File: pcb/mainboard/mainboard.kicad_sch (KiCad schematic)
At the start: 0 parts

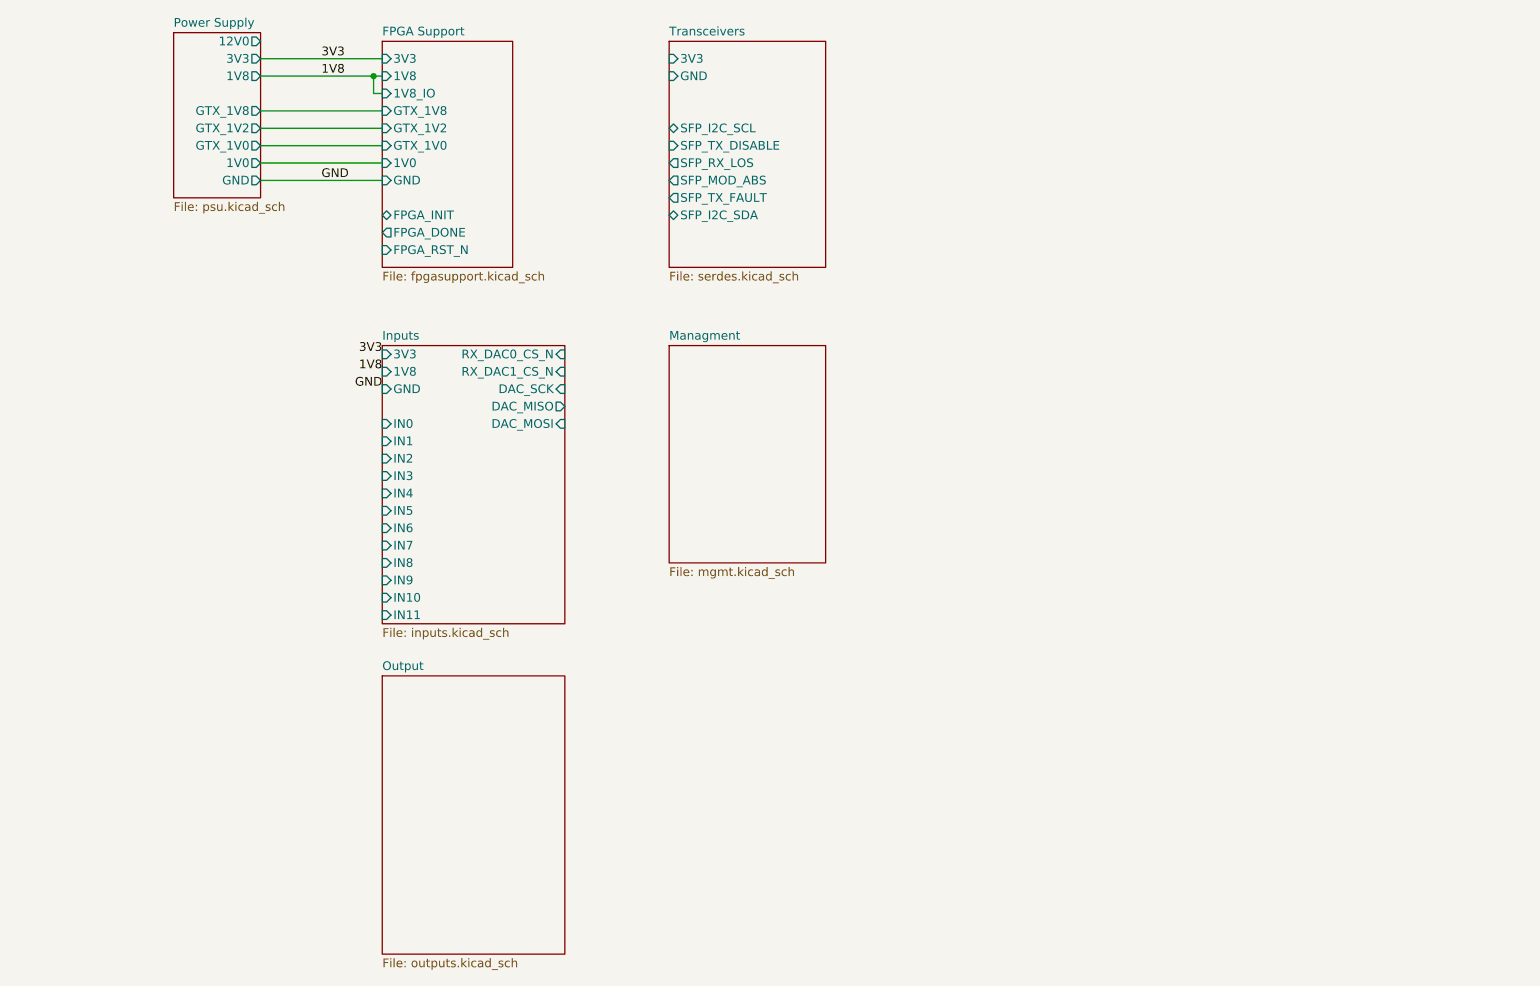
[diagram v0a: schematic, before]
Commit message: Continued initial work on main board
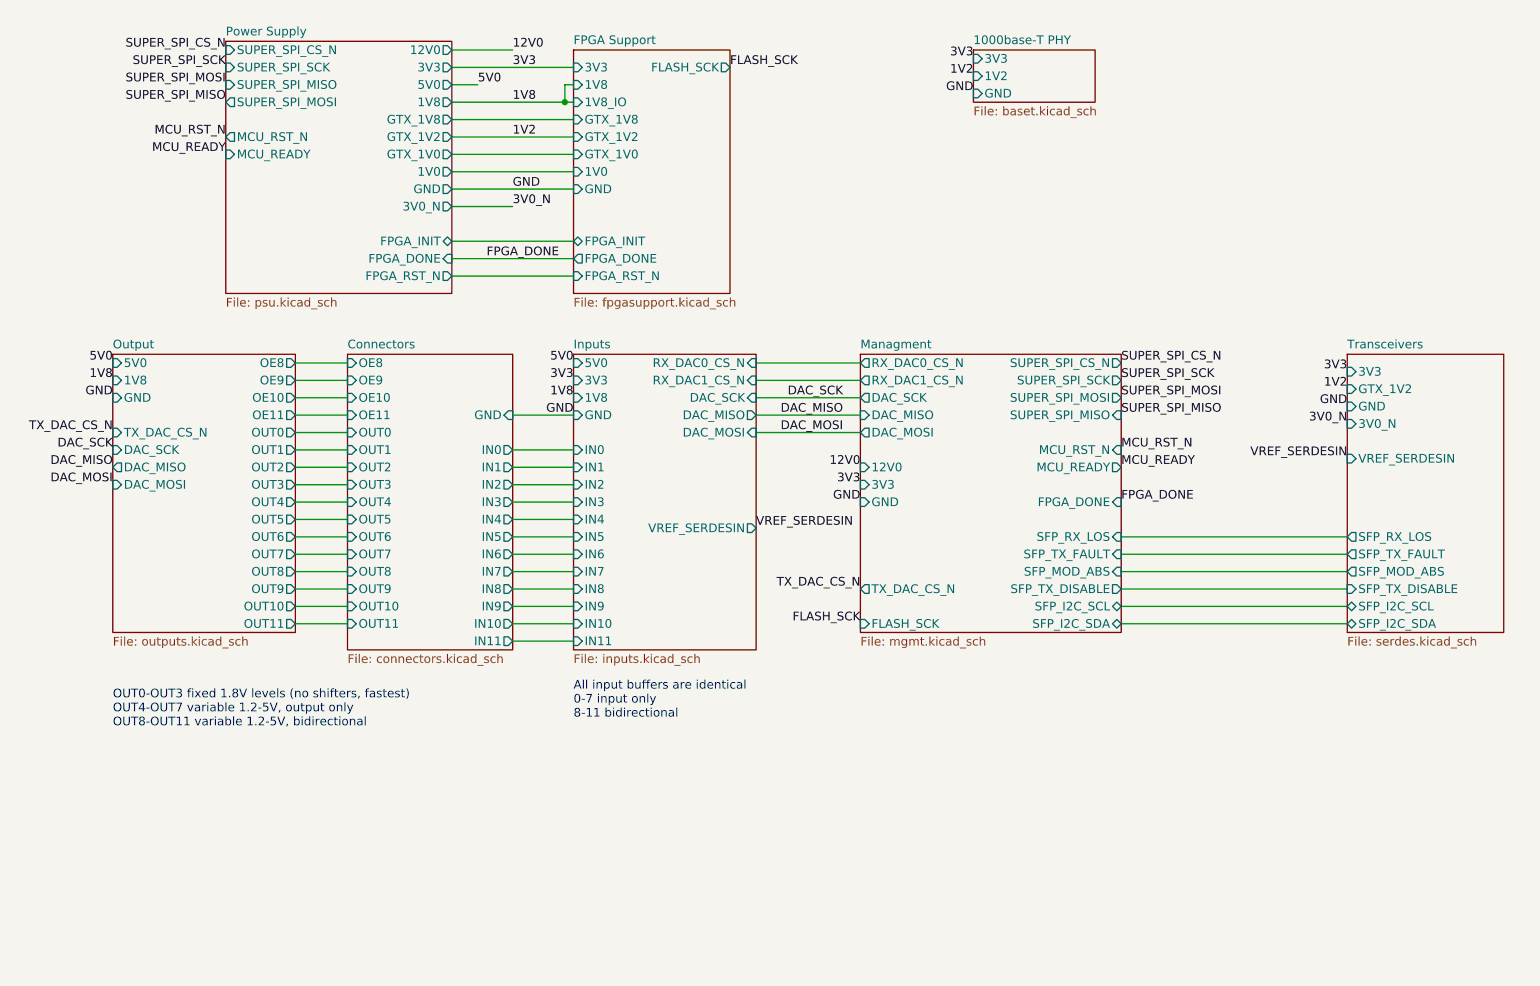
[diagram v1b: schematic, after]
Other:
- added sheet 1000base-T PHY (baset.kicad_sch)
- added sheet Connectors (connectors.kicad_sch)
- sheet FPGA Support ports: added FLASH_SCK; removed none
- sheet Inputs ports: added 5V0, VREF_SERDESIN; removed none
- sheet Managment ports: added 12V0, 3V3, DAC_MISO, DAC_MOSI, DAC_SCK, FLASH_SCK, FPGA_DONE, GND, MCU_READY, MCU_RST_N, RX_DAC0_CS_N, RX_DAC1_CS_N, SFP_I2C_SCL, SFP_I2C_SDA, SFP_MOD_ABS, SFP_RX_LOS, SFP_TX_DISABLE, SFP_TX_FAULT, SUPER_SPI_CS_N, SUPER_SPI_MISO, SUPER_SPI_MOSI, SUPER_SPI_SCK, TX_DAC_CS_N; removed none
- sheet Output ports: added 1V8, 5V0, DAC_MISO, DAC_MOSI, DAC_SCK, GND, OE10, OE11, OE8, OE9, OUT0, OUT1, OUT10, OUT11, OUT2, OUT3, OUT4, OUT5, OUT6, OUT7, OUT8, OUT9, TX_DAC_CS_N; removed none
- sheet Power Supply ports: added 3V0_N, 5V0, FPGA_DONE, FPGA_INIT, FPGA_RST_N, MCU_READY, MCU_RST_N, SUPER_SPI_CS_N, SUPER_SPI_MISO, SUPER_SPI_MOSI, SUPER_SPI_SCK; removed none
- sheet Transceivers ports: added 3V0_N, GTX_1V2, VREF_SERDESIN; removed none
- note added: "All input buffers are identical 0-7 input only 8-11 bidirectional"
- note added: "OUT0-OUT3 fixed 1.8V levels (no shifters, fastest) OUT4-OUT7 variable 1.2-5V, output only OUT8-OUT11 variable 1.2-5V, bidirectional"

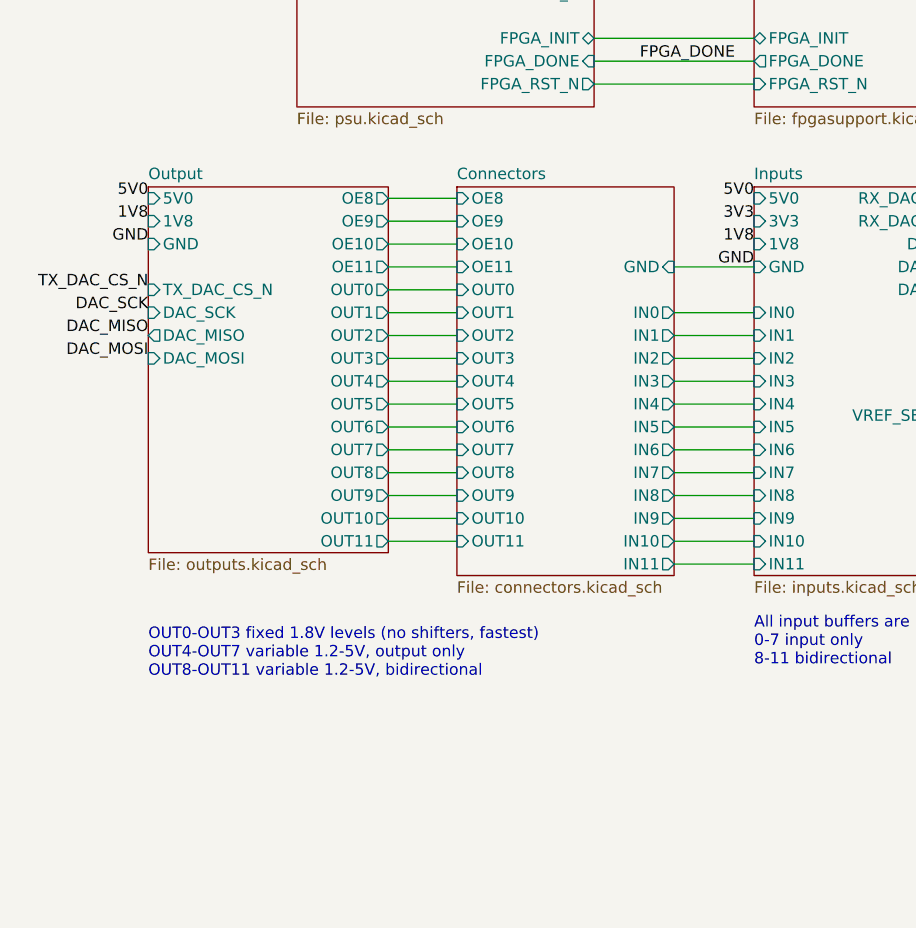
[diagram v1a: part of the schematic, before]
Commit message: Finished initial iteration of schematic, needs a verification pass to check for missing features then schematic review
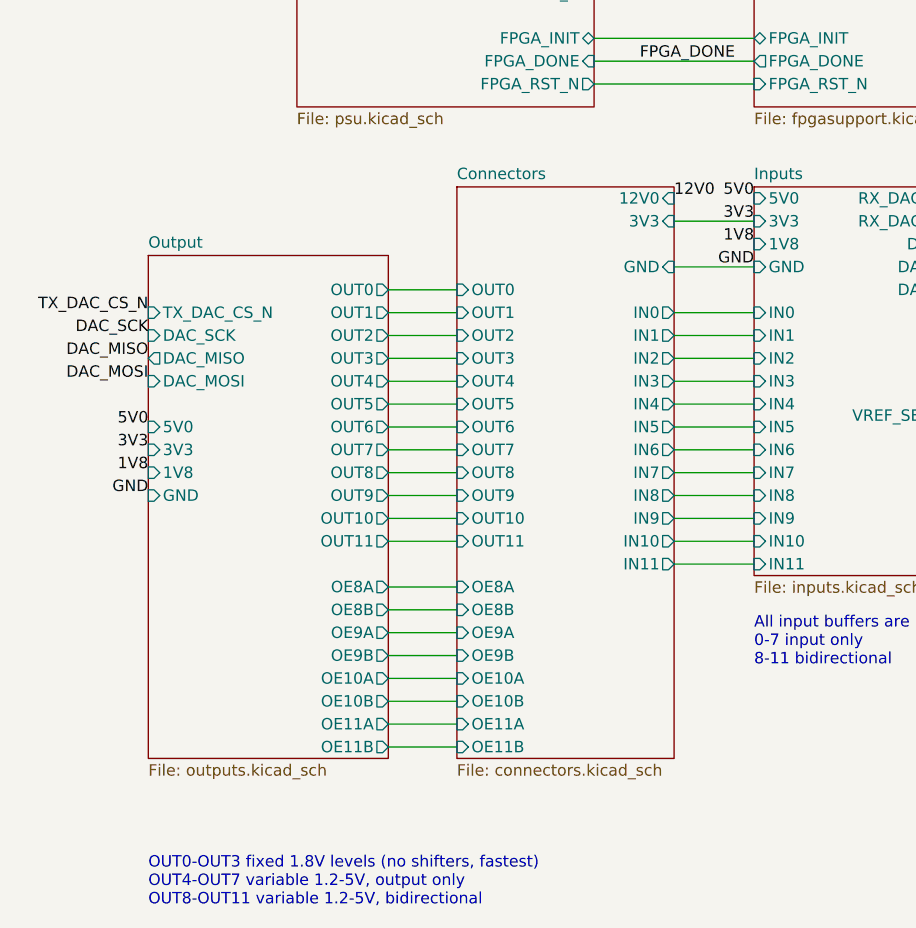
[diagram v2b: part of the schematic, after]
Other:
- sheet Connectors ports: added 12V0, 3V3, OE10A, OE10B, OE11A, OE11B, OE8A, OE8B, OE9A, OE9B; removed OE10, OE11, OE8, OE9
- sheet Output ports: added 3V3, OE10A, OE10B, OE11A, OE11B, OE8A, OE8B, OE9A, OE9B; removed OE10, OE11, OE8, OE9
- company: (none) -> Antikernel Labs
- title: (none) -> Trigger Crossbar

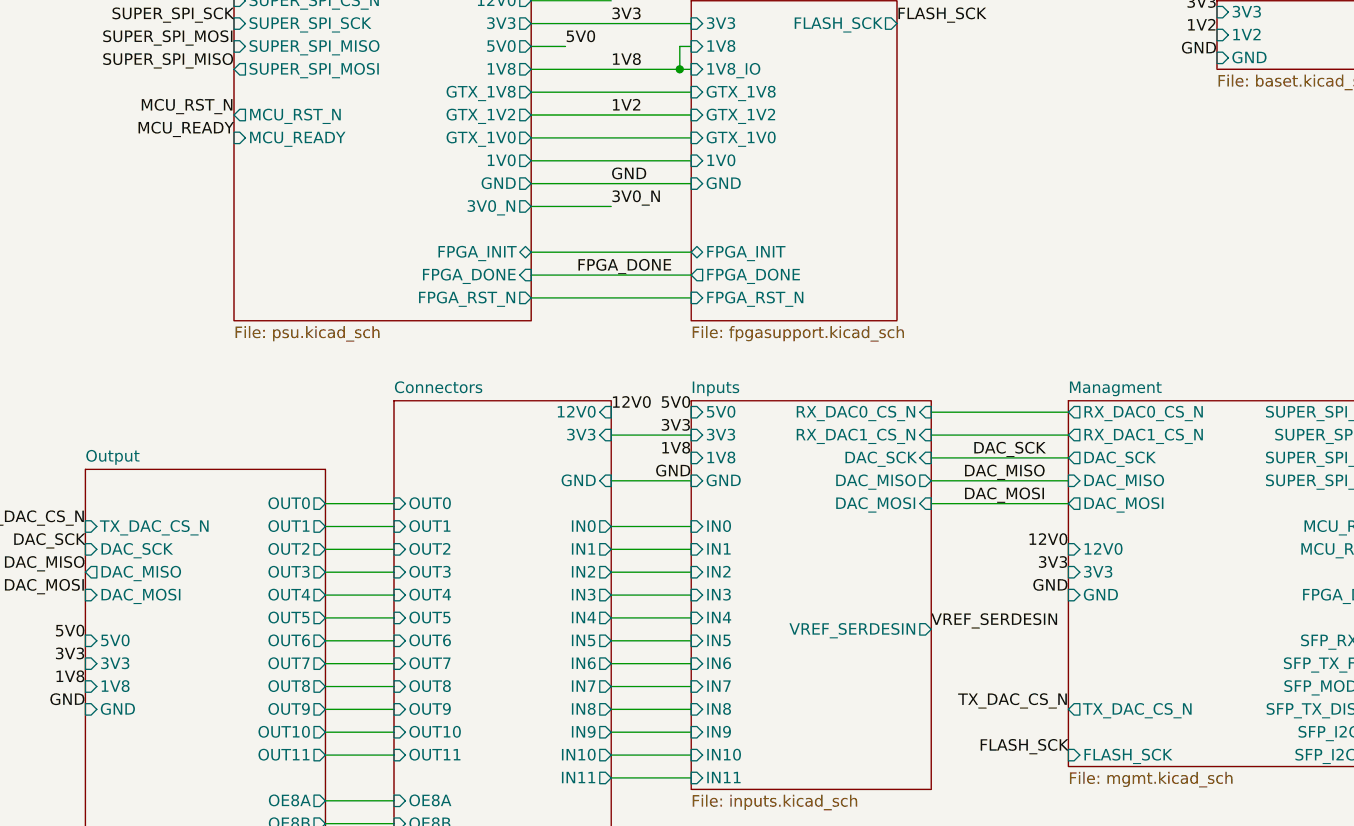
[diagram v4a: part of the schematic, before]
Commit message: Fixed typo, changed MCU Vbat to run on 3V3_SB
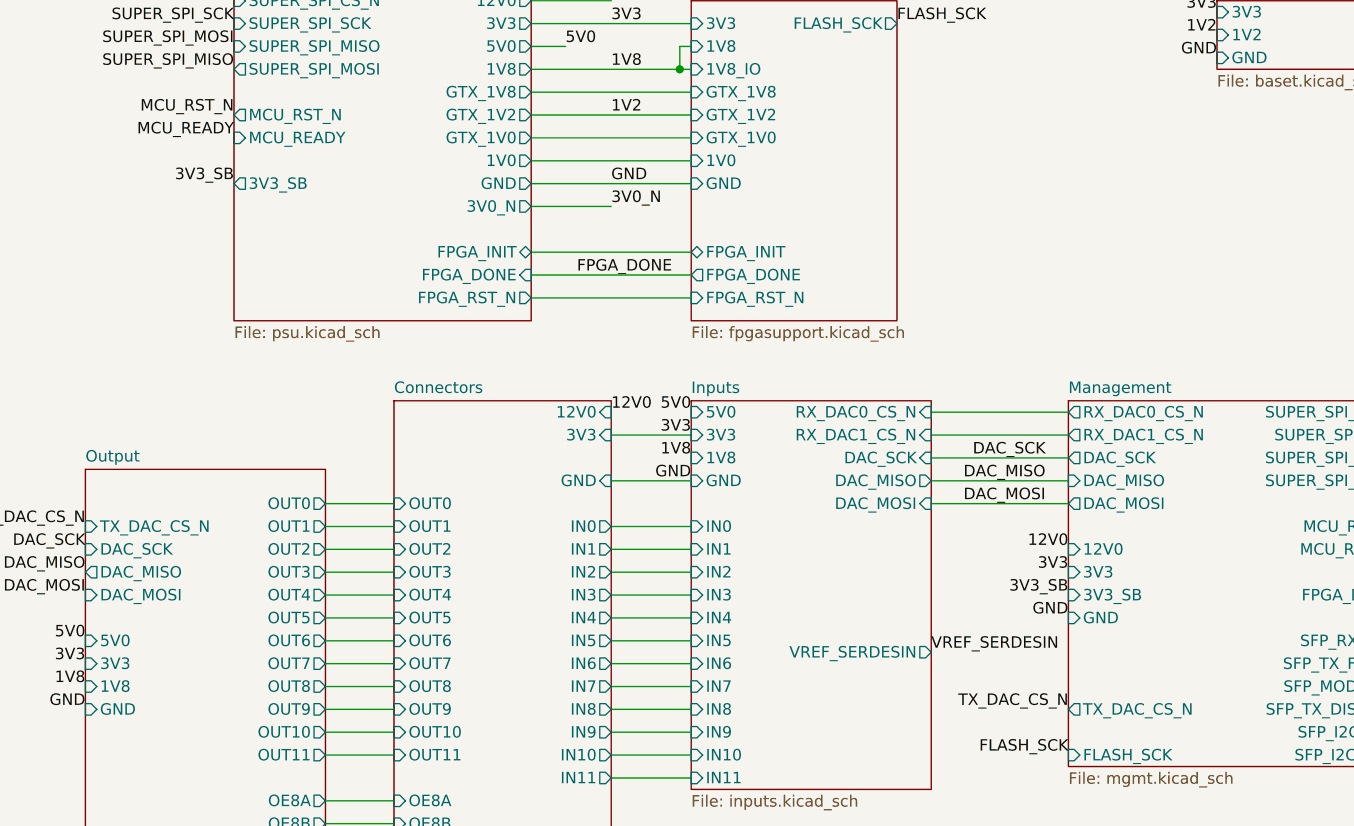
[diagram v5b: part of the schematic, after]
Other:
- sheet Managment renamed Management
- sheet Management ports: added 3V3_SB; removed none
- sheet Power Supply ports: added 3V3_SB; removed none
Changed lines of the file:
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@@
     (effects (font (size 1.27 1.27)) (justify right bottom))
   )
-  (label "GND" (at 135.89 90.17 180)
+  (label "GND" (at 135.89 92.71 180)
     (effects (font (size 1.27 1.27)) (justify right bottom))
   )
@@
     (effects (font (size 1.27 1.27)) (justify left bottom))
   )
+  (label "3V3_SB" (at 135.89 90.17 180)
+    (effects (font (size 1.27 1.27)) (justify right bottom))
+  )
   (label "FLASH_SCK" (at 116.84 26.67 0)
     (effects (font (size 1.27 1.27)) (justify left bottom))
@@
     (effects (font (size 1.27 1.27)) (justify right bottom))
   )
-  (label "VREF_SERDESIN" (at 120.65 93.98 0)
+  (label "VREF_SERDESIN" (at 120.65 96.52 0)
     (effects (font (size 1.27 1.27)) (justify left bottom))
   )
@@
   )
   (label "1V2" (at 207.01 73.66 180)
+    (effects (font (size 1.27 1.27)) (justify right bottom))
+  )
+  (label "3V3_SB" (at 43.18 44.45 180)
     (effects (font (size 1.27 1.27)) (justify right bottom))
   )
@@
     (stroke (width 0.1524) (type solid) (color 0 0 0 0))
     (fill (color 0 0 0 0.0000))
-    (property "Sheet name" "Managment" (id 0) (at 135.89 67.8684 0)
+    (property "Sheet name" "Management" (id 0) (at 135.89 67.8684 0)
       (effects (font (size 1.27 1.27)) (justify left bottom))
     )
@@
       (effects (font (size 1.27 1.27)) (justify left top))
     )
-    (pin "GND" input (at 135.89 90.17 180)
+    (pin "GND" input (at 135.89 92.71 180)
       (effects (font (size 1.27 1.27)) (justify left))
     )
@@
     )
     (pin "TX_DAC_CS_N" output (at 135.89 102.87 180)
+      (effects (font (size 1.27 1.27)) (justify left))
+    )
+    (pin "3V3_SB" input (at 135.89 90.17 180)
       (effects (font (size 1.27 1.27)) (justify left))
     )
@@
       (effects (font (size 1.27 1.27)) (justify right))
     )
+    (pin "3V3_SB" output (at 43.18 44.45 180)
+      (effects (font (size 1.27 1.27)) (justify left))
+    )
   )
   (sheet (at 26.67 76.2) (size 26.67 55.88) (fields_autoplaced)
@@
       (effects (font (size 1.27 1.27)) (justify right))
     )
-    (pin "VREF_SERDESIN" output (at 120.65 93.98 0)
-      (effects (font (size 1.27 1.27)) (justify right))
-    )
+    (pin "VREF_SERDESIN" output (at 120.65 96.52 0)
+      (effects (font (size 1.27 1.27)) (justify right))
+    )

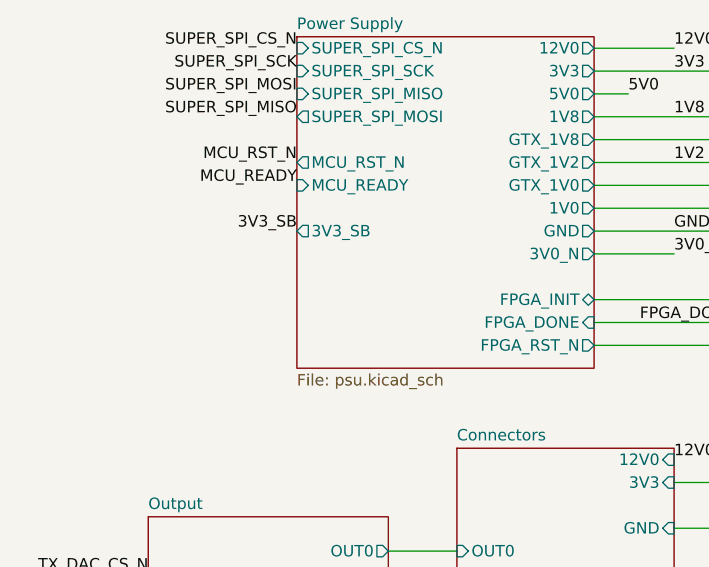
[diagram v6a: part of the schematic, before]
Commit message: Finished component footprint assignment, started some EM simulations. Ready for schematic review.
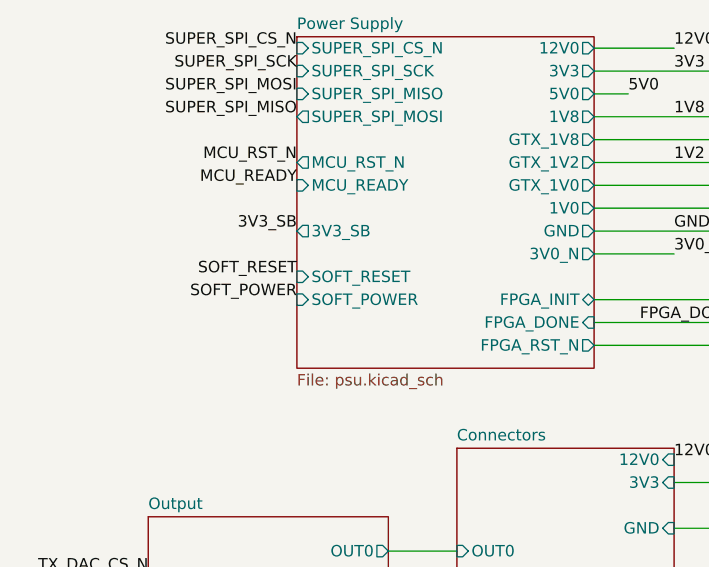
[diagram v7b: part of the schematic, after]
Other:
- sheet Power Supply ports: added SOFT_POWER, SOFT_RESET; removed none
